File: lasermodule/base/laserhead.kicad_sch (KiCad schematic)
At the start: 39 parts, among them J3 Conn_01x02, J4 Conn_01x03, J5 Conn_01x02, J6 jumper wire 2 pin, U1 DIGIPOT_50K, U11 LM7808_TO220, U2 U_IC-HKB, U3 STSPIN230, U4 MIC920, U5 MIC920, U6 DRV5033FAxDBZ, U7 DRV5033FAxDBZ, U8 DRV5033FAxDBZ

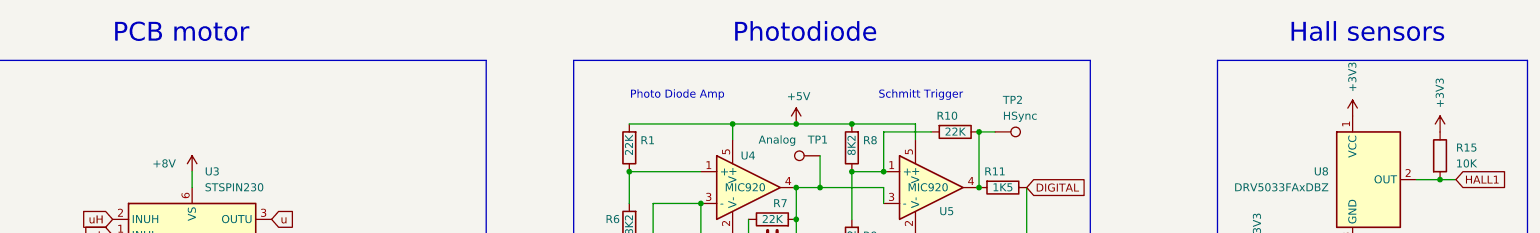
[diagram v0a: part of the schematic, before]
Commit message: added pcbmotor, renamed some folders
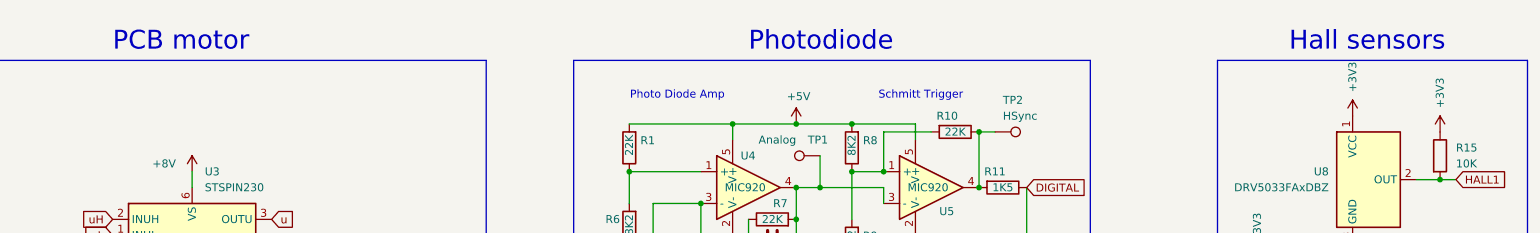
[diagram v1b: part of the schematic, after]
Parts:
- J4: footprint Connector_PinHeader_2.54mm:PinHeader_1x03_P2.54mm_Vertical -> sockets_scanhead:pcbmotor_smd
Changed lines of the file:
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@@
     (effects (font (size 1.27 1.27)) (justify left bottom))
   )
-  (text "PCB motor" (at 54.61 22.86 0)
+  (text "PCB motor" (at 54.61 24.13 0)
     (effects (font (size 3 3)) (justify left bottom))
   )
-  (text "Photodiode" (at 153.67 22.86 0)
+  (text "Photodiode" (at 156.21 24.13 0)
     (effects (font (size 3 3)) (justify left bottom))
   )
-  (text "Hall sensors" (at 242.57 22.86 0)
+  (text "Hall sensors" (at 242.57 24.13 0)
     (effects (font (size 3 3)) (justify left bottom))
   )
@@
       (effects (font (size 1.27 1.27)))
     )
-    (property "Footprint" "Connector_PinHeader_2.54mm:PinHeader_1x03_P2.54mm_Vertical" (at 97.79 64.77 0)
-      (effects (font (size 1.27 1.27)) hide)
-    )
+    (property "Footprint" "sockets_scanhead:pcbmotor_smd" (at 97.79 64.77 0)
+      (effects (font (size 1.27 1.27)) hide)
+    )

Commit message: further cleaned up and tested renders in blender
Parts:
- U3: footprint Package_DFN_QFN:VQFN-16-1EP_3x3mm_P0.5mm_EP1.8x1.8mm -> sockets_scanhead:VQFN-16-1EP_3x3mm_P0.5mm_EP1.8x1.8mm

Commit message: started adding other plates
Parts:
- J3, J5: footprint Connector_PinHeader_2.54mm:PinHeader_1x02_P2.54mm_Vertical -> sockets_scanhead:PinHeader_1x02_P2.54mm_Vertical
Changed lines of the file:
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@@
       (effects (font (size 1.27 1.27)) (justify left))
     )
-    (property "Footprint" "Connector_PinHeader_2.54mm:PinHeader_1x02_P2.54mm_Vertical" (at 162.56 77.47 0)
+    (property "Footprint" "sockets_scanhead:PinHeader_1x02_P2.54mm_Vertical" (at 162.56 77.47 0)
       (effects (font (size 1.27 1.27)) hide)
     )
@@
       (effects (font (size 1.27 1.27)) (justify left))
     )
-    (property "Footprint" "Connector_PinHeader_2.54mm:PinHeader_1x02_P2.54mm_Vertical" (at 148.59 77.47 0)
+    (property "Footprint" "sockets_scanhead:PinHeader_1x02_P2.54mm_Vertical" (at 148.59 77.47 0)
       (effects (font (size 1.27 1.27)) hide)
     )
